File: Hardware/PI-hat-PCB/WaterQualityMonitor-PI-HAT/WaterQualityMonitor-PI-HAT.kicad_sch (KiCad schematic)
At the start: 35 parts

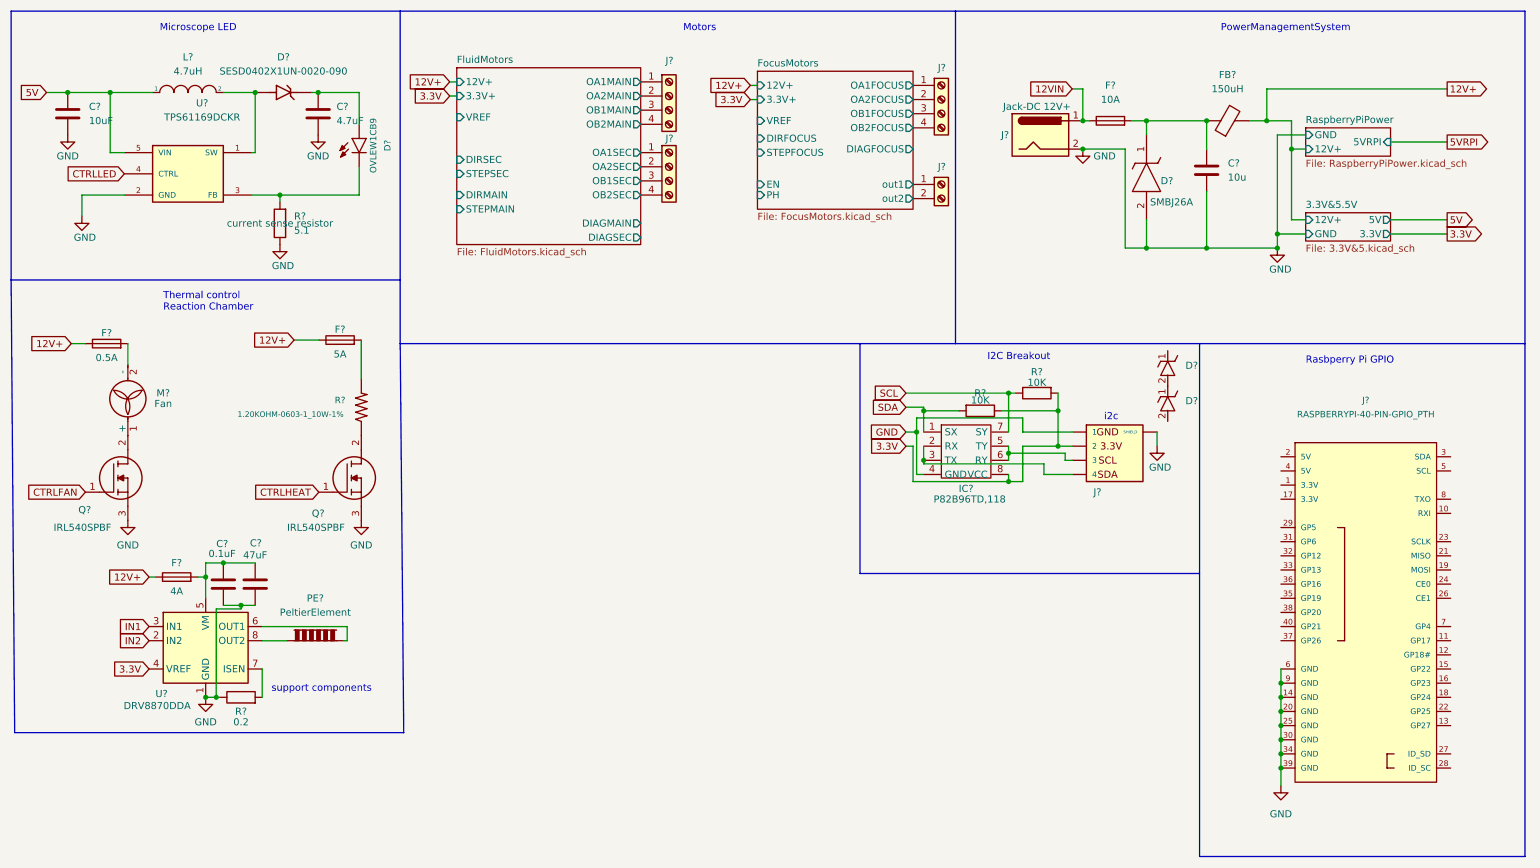
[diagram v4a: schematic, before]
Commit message: RPI integration
Connected RPI to all motors, sensors etc.
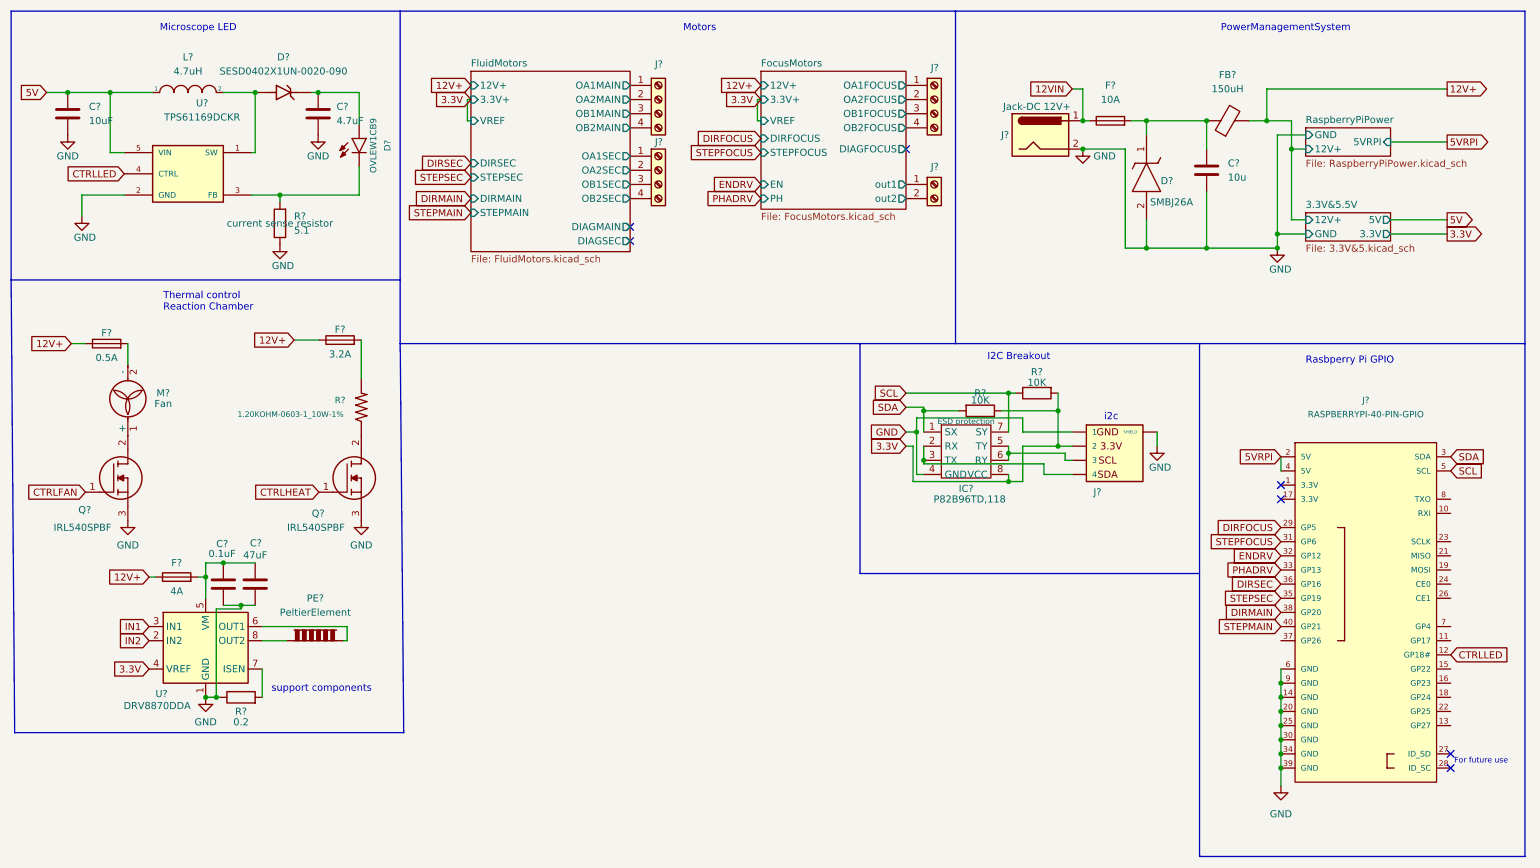
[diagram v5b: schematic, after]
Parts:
- removed D? (x2): VESD01C1-02V-G3-08, SODFL1608X70N, symbol SamacSys_Parts:VESD01C1-02V-G3-08
- F?: value 5A -> 3.2A
- IC?: Purpose (none) -> ESD protection
- J?: value RASPBERRYPI-40-PIN-GPIO_PTH -> RASPBERRYPI-40-PIN-GPIO
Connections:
- net 5VRPI: now also J?.2 (5V), J?.4 (5V)
- net CTRLLED: now also J?.12 (GP18#)
- net SCL: now also J?.5 (SCL)
- net SDA: now also J?.3 (SDA)
- net DIRFOCUS: now reaches J?.29 (GP5)
- net STEPFOCUS: now reaches J?.31 (GP6)
- net ENDRV: now reaches J?.32 (GP12)
- net PHADRV: now reaches J?.33 (GP13)
- net STEPSEC: now reaches J?.35 (GP19)
- net DIRSEC: now reaches J?.36 (GP16)
- net DIRMAIN: now reaches J?.38 (GP20)
- net STEPMAIN: now reaches J?.40 (GP21)
- no-connect marks 0 -> 7
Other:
- note added: "For future use"
- moved on the sheet: J?

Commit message: finished RPI integration
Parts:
- removed J?: Screw_Terminal_01x04, symbol Connector:Screw_Terminal_01x04
- added J?: Screw_Terminal_01x04, symbol Connector:Screw_Terminal_01x04
- added J? (x2): Conn_01x05_Male, symbol Connector:Conn_01x05_Male
- added J? (x2): Conn_01x02_Male, symbol Connector:Conn_01x02_Male
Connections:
- net FluidMotors/OA1MAIN: now also J?.1 (Pin_1)
- net FluidMotors/OA2MAIN: now also J?.2 (Pin_2)
- net FluidMotors/OB1MAIN: now also J?.3 (Pin_3)
- net FluidMotors/OB2MAIN: now also J?.4 (Pin_4)
- net at J?.10 (RXI): now also J?.1 (Pin_1)
- net at J?.11 (GP17): now also J?.1 (Pin_1)
- net at J?.13 (GP27): now also J?.1 (Pin_1)
- net at J?.15 (GP22): now also J?.5 (Pin_5)
- net at J?.16 (GP23): now also J?.4 (Pin_4)
- net at J?.18 (GP24): now also J?.3 (Pin_3)
- net at J?.19 (MOSI): now also J?.3 (Pin_3)
- net at J?.21 (MISO): now also J?.4 (Pin_4)
- net at J?.22 (GP25): now also J?.2 (Pin_2)
- net at J?.23 (SCLK): now also J?.5 (Pin_5)
- net at J?.24 (CE0): now also J?.2 (Pin_2)
- net at J?.26 (CE1): now also J?.1 (Pin_1)
- net at J?.7 (GP4): now also J?.2 (Pin_2)
- net at J?.8 (TXO): now also J?.2 (Pin_2)
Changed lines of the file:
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@@
     (stroke (width 0) (type default) (color 0 0 0 0))
   )
-  (wire (pts (xy 63.5 71.755) (xy 67.945 71.755))
+  (wire (pts (xy 64.135 71.755) (xy 67.945 71.755))
     (stroke (width 0) (type default) (color 0 0 0 0))
   )
@@
     )
   )
-  (global_label "12V+" (shape input) (at 63.5 71.755 180) (fields_autoplaced)
-    (effects (font (size 1.27 1.27)) (justify right))
-    (property "Intersheet References" "${INTERSHEET_REFS}" (id 0) (at 56.0069 71.6756 0)
+  (global_label "12V+" (shape input) (at 64.135 71.755 180) (fields_autoplaced)
+    (effects (font (size 1.27 1.27)) (justify right))
+    (property "Intersheet References" "${INTERSHEET_REFS}" (id 0) (at 56.6419 71.6756 0)
       (effects (font (size 1.27 1.27)) (justify right) hide)
     )
@@
     (pin "1")
   )
+  (symbol (lib_id "Connector:Screw_Terminal_01x04") (at 128.905 28.575 0) (unit 1)
+    (in_bom yes) (on_board yes)
+    (property "Reference" "J?" (id 0) (at 128.27 23.495 0)
+      (effects (font (size 1.27 1.27)) (justify left))
+    )
+    (property "Value" "Screw_Terminal_01x04" (id 1) (at 131.445 31.1149 0)
+      (effects (font (size 1.27 1.27)) (justify left) hide)
+    )
+    (property "Footprint" "" (id 2) (at 128.905 28.575 0)
+      (effects (font (size 1.27 1.27)) hide)
+    )
+    (property "Datasheet" "~" (id 3) (at 128.905 28.575 0)
+      (effects (font (size 1.27 1.27)) hide)
+    )
+    (pin "1")
+    (pin "2")
+    (pin "3")
+    (pin "4")
+  )
   (symbol (lib_id "power:GND") (at 25.4 49.53 0) (unit 1)
     (in_bom yes) (on_board yes) (fields_autoplaced)
@@
     (pin "2")
   )
+  (symbol (lib_id "Connector:Conn_01x05_Male") (at 276.225 135.89 180) (unit 1)
+    (in_bom yes) (on_board yes) (fields_autoplaced)
+    (property "Reference" "J?" (id 0) (at 278.13 135.8899 0)
+      (effects (font (size 1.27 1.27)) (justify right))
+    )
+    (property "Value" "Conn_01x05_Male" (id 1) (at 278.13 137.1599 0)
+      (effects (font (size 1.27 1.27)) (justify right) hide)
+    )
+    (property "Footprint" "" (id 2) (at 276.225 135.89 0)
+      (effects (font (size 1.27 1.27)) hide)
+    )
+    (property "Datasheet" "~" (id 3) (at 276.225 135.89 0)
+      (effects (font (size 1.27 1.27)) hide)
+    )
+    (pin "1")
+    (pin "2")
+    (pin "3")
+    (pin "4")
+    (pin "5")
+  )
   (symbol (lib_id "SamacSys_Parts:IRL540SPBF") (at 67.945 99.06 0) (unit 1)
     (in_bom yes) (on_board yes)
@@
     (pin "2")
   )
-  (symbol (lib_id "Connector:Screw_Terminal_01x04") (at 128.905 28.575 0) (unit 1)
-    (in_bom yes) (on_board yes)
-    (property "Reference" "J?" (id 0) (at 128.27 22.225 0)
-      (effects (font (size 1.27 1.27)) (justify left))
-    )
-    (property "Value" "Screw_Terminal_01x04" (id 1) (at 131.445 31.1149 0)
-      (effects (font (size 1.27 1.27)) (justify left) hide)
-    )
-    (property "Footprint" "" (id 2) (at 128.905 28.575 0)
-      (effects (font (size 1.27 1.27)) hide)
-    )
-    (property "Datasheet" "~" (id 3) (at 128.905 28.575 0)
+  (symbol (lib_id "Connector:Conn_01x05_Male") (at 276.225 113.03 180) (unit 1)
+    (in_bom yes) (on_board yes) (fields_autoplaced)
+    (property "Reference" "J?" (id 0) (at 278.13 113.0299 0)
+      (effects (font (size 1.27 1.27)) (justify right))
+    )
+    (property "Value" "Conn_01x05_Male" (id 1) (at 278.13 114.2999 0)
+      (effects (font (size 1.27 1.27)) (justify right) hide)
+    )
+    (property "Footprint" "" (id 2) (at 276.225 113.03 0)
+      (effects (font (size 1.27 1.27)) hide)
+    )
+    (property "Datasheet" "~" (id 3) (at 276.225 113.03 0)
       (effects (font (size 1.27 1.27)) hide)
     )
@@
     (pin "3")
     (pin "4")
+    (pin "5")
   )
   (symbol (lib_id "Connector:Screw_Terminal_01x02") (at 178.435 43.815 0) (unit 1)
@@
     (pin "2")
   )
+  (symbol (lib_id "Connector:Conn_01x02_Male") (at 276.225 102.87 180) (unit 1)
+    (in_bom yes) (on_board yes) (fields_autoplaced)
+    (property "Reference" "J?" (id 0) (at 278.13 101.5999 0)
+      (effects (font (size 1.27 1.27)) (justify right))
+    )
+    (property "Value" "Conn_01x02_Male" (id 1) (at 278.13 102.8699 0)
+      (effects (font (size 1.27 1.27)) (justify right) hide)
+    )
+    (property "Footprint" "" (id 2) (at 276.225 102.87 0)
+      (effects (font (size 1.27 1.27)) hide)
+    )
+    (property "Datasheet" "~" (id 3) (at 276.225 102.87 0)
+      (effects (font (size 1.27 1.27)) hide)
+    )
+    (pin "1")
+    (pin "2")
+  )
   (symbol (lib_id "power:GND") (at 47.625 135.89 0) (unit 1)
     (in_bom yes) (on_board yes)
@@
     )
     (pin "1")
+  )
+  (symbol (lib_id "Connector:Conn_01x02_Male") (at 276.225 125.73 180) (unit 1)
+    (in_bom yes) (on_board yes) (fields_autoplaced)
+    (property "Reference" "J?" (id 0) (at 278.13 124.4599 0)
+      (effects (font (size 1.27 1.27)) (justify right))
+    )
+    (property "Value" "Conn_01x02_Male" (id 1) (at 278.13 125.7299 0)
+      (effects (font (size 1.27 1.27)) (justify right) hide)
+    )
+    (property "Footprint" "" (id 2) (at 276.225 125.73 0)
+      (effects (font (size 1.27 1.27)) hide)
+    )
+    (property "Datasheet" "~" (id 3) (at 276.225 125.73 0)
+      (effects (font (size 1.27 1.27)) hide)
+    )
+    (pin "1")
+    (pin "2")
   )
   (symbol (lib_id "Device:C") (at 67.818 31.115 0) (unit 1)
@@
     )
     (path "/7b03732c-6b0a-482e-b8e3-ced6ad7436b5/6404ccb8-58f1-49b5-b309-15fc332ead6d"
-      (reference "#PWR?") (unit 1) (value "GND") (footprint "")
+      (reference "#PWR0128") (unit 1) (value "GND") (footprint "")
     )
     (path "/023fab8f-e850-4f6d-bd01-c197d7adaf26"
@@
       (reference "J?") (unit 1) (value "Screw_Terminal_01x04") (footprint "")
     )
-    (path "/56e6d351-4e40-4a46-8382-9fdba54bb8cf"
+    (path "/31524668-8e36-4ca7-9ad5-0186c36bd019"
       (reference "J?") (unit 1) (value "Screw_Terminal_01x04") (footprint "")
+    )
+    (path "/48fc8de1-5b68-4d42-8544-2aec0a71bf17"
+      (reference "J?") (unit 1) (value "Conn_01x05_Male") (footprint "")
+    )
+    (path "/58f0af31-b75f-4665-8205-44777b5f3606"
+      (reference "J?") (unit 1) (value "Conn_01x05_Male") (footprint "")
     )
     (path "/5aac9ea9-4fe8-4ec4-82c6-ee5bf07b1349"
@@
       (reference "J?") (unit 1) (value "RASPBERRYPI-40-PIN-GPIO") (footprint "2X20_SHROUDED")
     )
+    (path "/8c0d1ce8-b9c5-4405-ad31-fbd575f1bcad"
+      (reference "J?") (unit 1) (value "Conn_01x02_Male") (footprint "")
+    )
+    (path "/9e7997e2-c317-4671-a90c-3f03f74b917d"
+      (reference "J?") (unit 1) (value "Conn_01x02_Male") (footprint "")
+    )
     (path "/a59c5d3d-4ea0-4b08-99c1-38f965204418"

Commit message: enhanced layout
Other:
- moved on the sheet: F?, IC?, J?, M?, Q?, R?

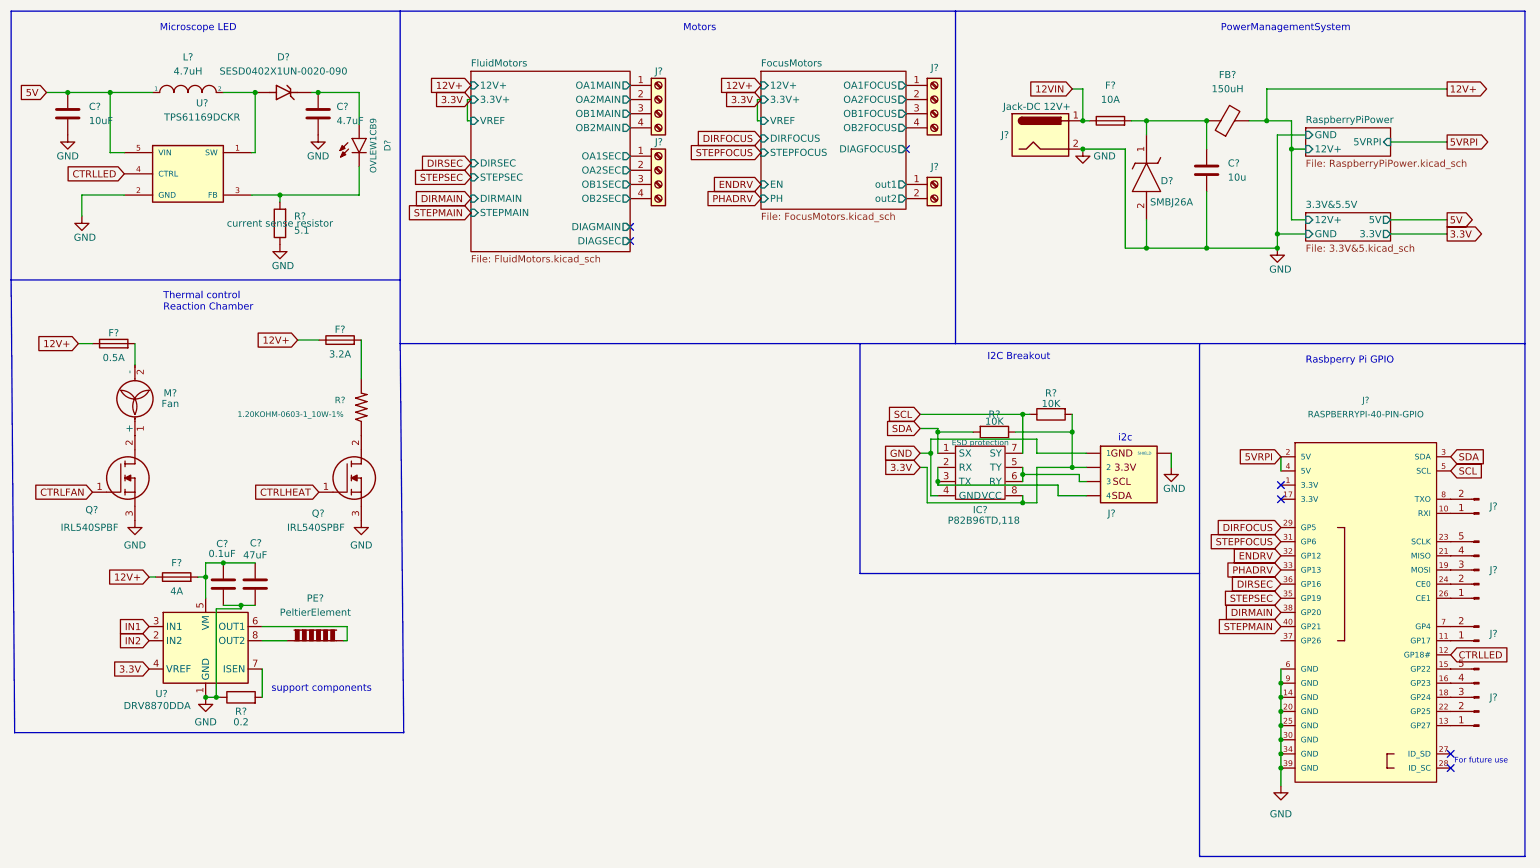
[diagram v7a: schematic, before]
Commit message: assigent footprints to all current components
I chose 1206smd handsolderable for caps and resistors and inductors, may need to be revised
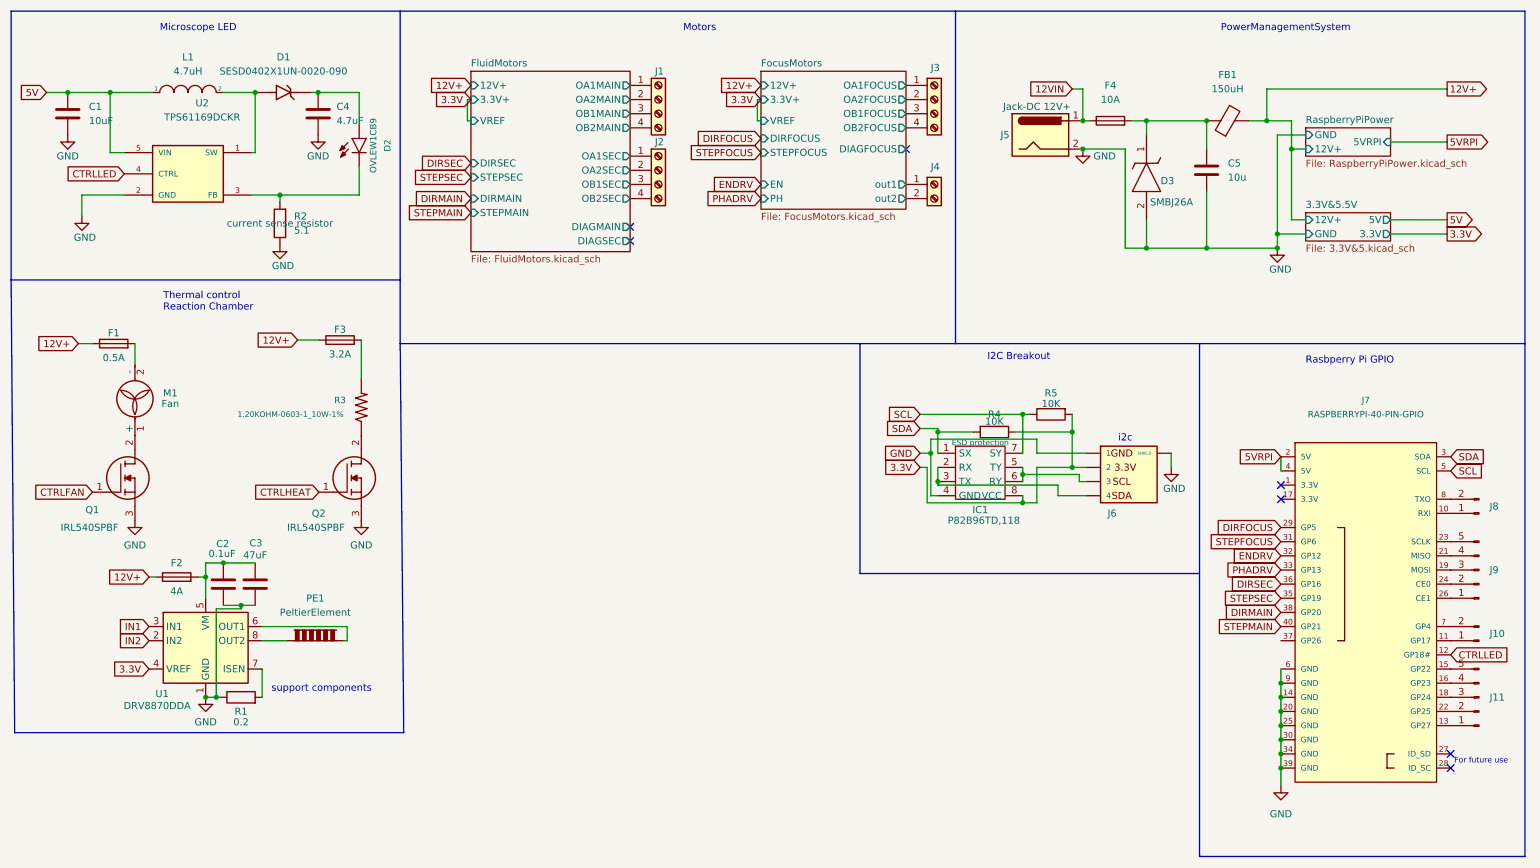
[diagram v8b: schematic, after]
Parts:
- C1: renamed from C?; footprint (none) -> SmacSYs:SOIC127P600X175-8N
- C2, C3, C4, C5: renamed from C?; footprint (none) -> Capacitor_SMD:C_1206_3216Metric_Pad1.33x1.80mm_HandSolder
- D1: renamed from D?; footprint DIODFN100X60X43-2N -> SmacSYs:SESD0402X1UN0020090
- D2: renamed from D?; footprint LED_5MM -> SmacSYs:OVLEW1CB9
- D3: renamed from D?; footprint DIOM5436X244N -> Snapeda:DIOM4336X265N
- F1, F2, F3, F4: renamed from F?; footprint (none) -> Fuse:Fuse_1206_3216Metric_Pad1.42x1.75mm_HandSolder
- FB1: renamed from FB?; footprint (none) -> Inductor_SMD:L_1206_3216Metric_Pad1.22x1.90mm_HandSolder
- IC1: renamed from IC?; footprint SOIC127P600X175-8N -> SmacSYs:SOIC127P600X175-8N
- J1, J2, J3: renamed from J?; footprint (none) -> TerminalBlock:TerminalBlock_Altech_AK300-4_P5.00mm
- J10, J11, J8, J9: renamed from J?; footprint (none) -> Connector_PinHeader_2.54mm:PinHeader_1x02_P2.54mm_Vertical
- J4: renamed from J?; footprint (none) -> TerminalBlock:TerminalBlock_Altech_AK300-2_P5.00mm
- J5: renamed from J?; footprint (none) -> Connector_BarrelJack:BarrelJack_Wuerth_6941xx301002
- J6: renamed from J?; footprint JST_SM04B-SRSS-TB(LF)(SN) -> Snapeda:JST_SM04B-SRSS-TB(LF)(SN)
- J7: renamed from J?; footprint 2X20_SHROUDED -> Snapeda:MODULE_RASPBERRY_PI_3_MODEL_B+
- L1: renamed from L?; footprint (none) -> Inductor_SMD:L_1206_3216Metric_Pad1.22x1.90mm_HandSolder
- M1: renamed from M?; footprint (none) -> Connector_PinHeader_2.54mm:PinHeader_1x02_P2.54mm_Vertical
- PE1: renamed from PE?; footprint (none) -> TerminalBlock:TerminalBlock_Altech_AK300-2_P5.00mm
- Q1, Q2: renamed from Q?; footprint IRL540SPBF -> SmacSYs:IRL540SPBF
- R1, R2, R4, R5: renamed from R?; footprint (none) -> Resistor_SMD:R_1206_3216Metric_Pad1.30x1.75mm_HandSolder
- R3: renamed from R?; footprint 0603 -> Resistor_SMD:R_1206_3216Metric_Pad1.30x1.75mm_HandSolder
- U2: renamed from U?; footprint SOT65P210X110-5N -> Snapeda:SOT65P210X110-5N
- gave numbers to parts that had none: 1
